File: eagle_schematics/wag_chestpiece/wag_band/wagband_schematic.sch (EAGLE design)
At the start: 8 parts, among them U1 ATMEGA328P_PDIP, U2 TLV1117-33CDCY

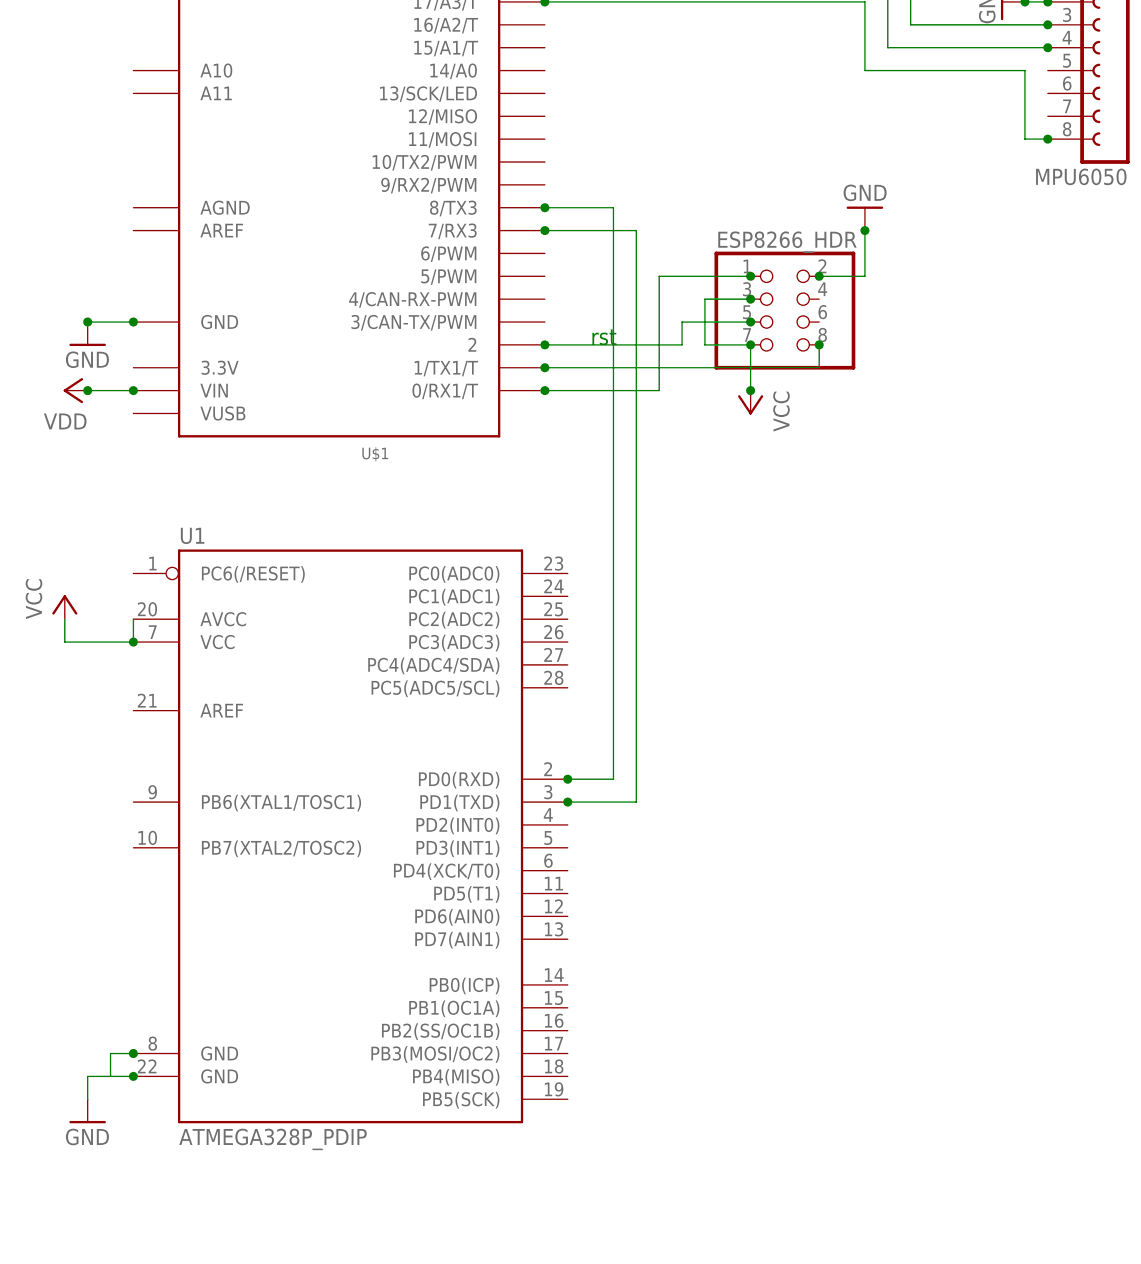
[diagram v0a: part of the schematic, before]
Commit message: Added EasyVR header to chestband
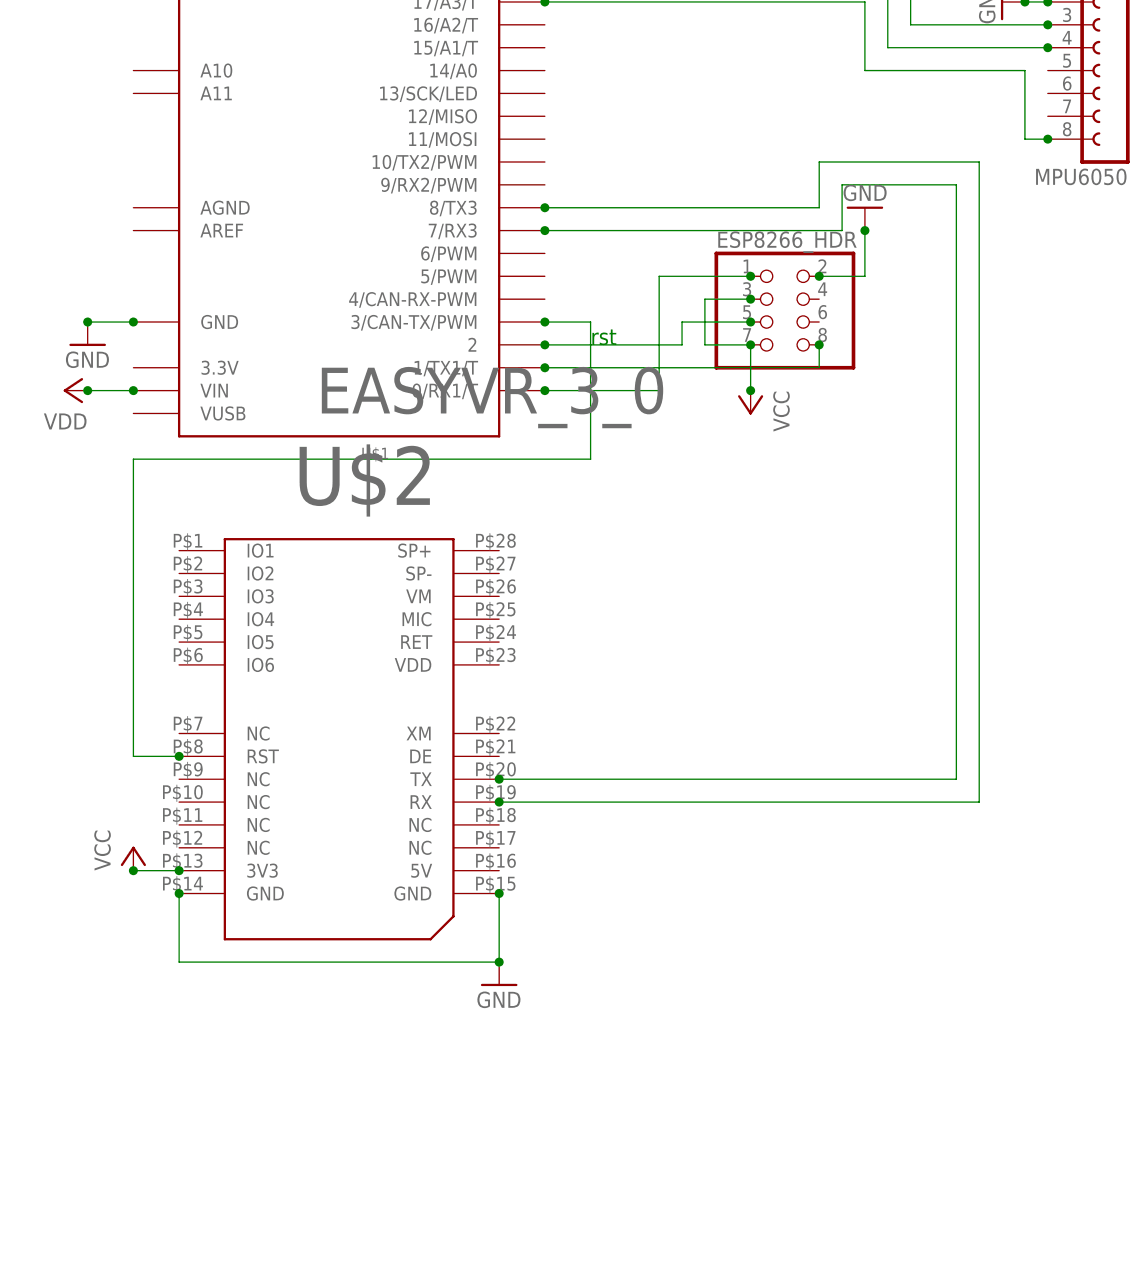
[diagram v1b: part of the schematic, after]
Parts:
- removed U1: ATMEGA328P_PDIP, SparkFun-DigitalIC:ATMEGA328P_PDIP
- added U$2: EASYVR_3_0, mqp_custom_parts:EASYVR_3_0
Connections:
- new net N$5: U$1.3/CAN-TX/PWM, U$2.RST
- net GND: now also U$2.GND@1, U$2.GND@2; no longer U1.GND@1, U1.GND@2
- net N$1: now also U$2.TX; no longer U1.PD1(TXD)
- net N$2: now also U$2.RX; no longer U1.PD0(RXD)
- net VCC: now also U$2.3V3; no longer U1.AVCC, U1.VCC
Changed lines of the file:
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@@
 <part name="GND7" library="supply1" deviceset="GND" device=""/>
 <part name="FRAME1" library="frames" deviceset="A4L-LOC" device="" value="10"/>
-<part name="U1" library="SparkFun-DigitalIC" deviceset="ATMEGA328P_PDIP" device=""/>
-<part name="GND1" library="supply1" deviceset="GND" device=""/>
-<part name="P+5" library="supply1" deviceset="VCC" device=""/>
+<part name="U$2" library="mqp_custom_parts" deviceset="EASYVR_3_0" device=""/>
+<part name="GND8" library="supply1" deviceset="GND" device=""/>
+<part name="P+1" library="supply1" deviceset="VCC" device=""/>
 </parts>
 <sheets>
@@
 <instance part="GND7" gate="1" x="160.02" y="142.24"/>
 <instance part="FRAME1" gate="G$1" x="0" y="0"/>
-<instance part="U1" gate="G$1" x="45.72" y="55.88"/>
-<instance part="GND1" gate="1" x="17.78" y="20.32"/>
-<instance part="P+5" gate="VCC" x="15.24" y="78.74"/>
+<instance part="U$2" gate="G$1" x="45.72" y="66.04"/>
+<instance part="GND8" gate="1" x="63.5" y="35.56"/>
+<instance part="P+1" gate="VCC" x="22.86" y="50.8"/>
 </instances>
 <busses>
@@
 </segment>
 <segment>
-<pinref part="U1" gate="G$1" pin="GND@1"/>
-<junction x="22.86" y="27.94"/>
-<wire x1="22.86" y1="27.94" x2="20.32" y2="27.94" width="0.1524" layer="91"/>
-<wire x1="20.32" y1="27.94" x2="20.32" y2="25.4" width="0.1524" layer="91"/>
-<pinref part="U1" gate="G$1" pin="GND@2"/>
-<junction x="22.86" y="25.4"/>
-<wire x1="20.32" y1="25.4" x2="22.86" y2="25.4" width="0.1524" layer="91"/>
-<wire x1="20.32" y1="25.4" x2="17.78" y2="25.4" width="0.1524" layer="91"/>
-<wire x1="17.78" y1="25.4" x2="17.78" y2="22.86" width="0.1524" layer="91"/>
-<pinref part="GND1" gate="1" pin="GND"/>
+<pinref part="U$2" gate="G$1" pin="GND@2"/>
+<wire x1="63.5" y1="45.72" x2="63.5" y2="38.1" width="0.1524" layer="91"/>
+<wire x1="63.5" y1="38.1" x2="27.94" y2="38.1" width="0.1524" layer="91"/>
+<pinref part="U$2" gate="G$1" pin="GND@1"/>
+<wire x1="27.94" y1="38.1" x2="27.94" y2="45.72" width="0.1524" layer="91"/>
+<junction x="27.94" y="45.72"/>
+<junction x="63.5" y="45.72"/>
+<pinref part="GND8" gate="1" pin="GND"/>
+<junction x="63.5" y="38.1"/>
 </segment>
 </net>
@@
 </segment>
 <segment>
-<pinref part="U1" gate="G$1" pin="VCC"/>
-<junction x="22.86" y="73.66"/>
-<pinref part="U1" gate="G$1" pin="AVCC"/>
-<wire x1="22.86" y1="76.2" x2="22.86" y2="73.66" width="0.1524" layer="91"/>
-<pinref part="P+5" gate="VCC" pin="VCC"/>
-<wire x1="22.86" y1="73.66" x2="15.24" y2="73.66" width="0.1524" layer="91"/>
-<wire x1="15.24" y1="73.66" x2="15.24" y2="76.2" width="0.1524" layer="91"/>
+<pinref part="P+1" gate="VCC" pin="VCC"/>
+<pinref part="U$2" gate="G$1" pin="3V3"/>
+<wire x1="22.86" y1="48.26" x2="27.94" y2="48.26" width="0.1524" layer="91"/>
+<junction x="22.86" y="48.26"/>
+<junction x="27.94" y="48.26"/>
 </segment>
 </net>
@@
 <segment>
 <pinref part="U$1" gate="G$1" pin="7/RX3"/>
-<wire x1="68.58" y1="119.38" x2="78.74" y2="119.38" width="0.1524" layer="91"/>
-<wire x1="78.74" y1="119.38" x2="78.74" y2="55.88" width="0.1524" layer="91"/>
-<pinref part="U1" gate="G$1" pin="PD1(TXD)"/>
-<wire x1="78.74" y1="55.88" x2="71.12" y2="55.88" width="0.1524" layer="91"/>
 <junction x="68.58" y="119.38"/>
-<junction x="71.12" y="55.88"/>
+<wire x1="68.58" y1="119.38" x2="101.6" y2="119.38" width="0.1524" layer="91"/>
+<wire x1="101.6" y1="119.38" x2="101.6" y2="124.46" width="0.1524" layer="91"/>
+<wire x1="101.6" y1="124.46" x2="114.3" y2="124.46" width="0.1524" layer="91"/>
+<wire x1="114.3" y1="124.46" x2="114.3" y2="58.42" width="0.1524" layer="91"/>
+<wire x1="114.3" y1="58.42" x2="63.5" y2="58.42" width="0.1524" layer="91"/>
+<pinref part="U$2" gate="G$1" pin="TX"/>
+<junction x="63.5" y="58.42"/>
 </segment>
 </net>
@@
 <segment>
 <pinref part="U$1" gate="G$1" pin="8/TX3"/>
-<wire x1="68.58" y1="121.92" x2="76.2" y2="121.92" width="0.1524" layer="91"/>
-<wire x1="76.2" y1="121.92" x2="76.2" y2="58.42" width="0.1524" layer="91"/>
-<pinref part="U1" gate="G$1" pin="PD0(RXD)"/>
-<wire x1="76.2" y1="58.42" x2="71.12" y2="58.42" width="0.1524" layer="91"/>
 <junction x="68.58" y="121.92"/>
-<junction x="71.12" y="58.42"/>
-</segment>
-</net>
+<wire x1="68.58" y1="121.92" x2="99.06" y2="121.92" width="0.1524" layer="91"/>
+<wire x1="99.06" y1="121.92" x2="99.06" y2="127" width="0.1524" layer="91"/>
+<wire x1="99.06" y1="127" x2="116.84" y2="127" width="0.1524" layer="91"/>
+<wire x1="116.84" y1="127" x2="116.84" y2="55.88" width="0.1524" layer="91"/>
+<pinref part="U$2" gate="G$1" pin="RX"/>
+<wire x1="116.84" y1="55.88" x2="63.5" y2="55.88" width="0.1524" layer="91"/>
+<junction x="63.5" y="55.88"/>
+</segment>
+</net>
+<net name="N$5" class="0">
+<segment>
+<pinref part="U$1" gate="G$1" pin="3/CAN-TX/PWM"/>
+<junction x="68.58" y="109.22"/>
+<wire x1="68.58" y1="109.22" x2="73.66" y2="109.22" width="0.1524" layer="91"/>
+<wire x1="73.66" y1="109.22" x2="73.66" y2="93.98" width="0.1524" layer="91"/>
+<wire x1="73.66" y1="93.98" x2="22.86" y2="93.98" width="0.1524" layer="91"/>
+<wire x1="22.86" y1="93.98" x2="22.86" y2="60.96" width="0.1524" layer="91"/>
+<pinref part="U$2" gate="G$1" pin="RST"/>
+<junction x="27.94" y="60.96"/>
+<wire x1="22.86" y1="60.96" x2="27.94" y2="60.96" width="0.1524" layer="91"/>
+</segment>
+</net>

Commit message: Added more parts for eagle
Finished PCBs
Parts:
- removed BATTERY: (no value), adafruit:JST_2PIN-THM-RA
- removed ESP8266_HDR: (no value), pinhead:PINHD-2X4
- removed MPU6050: (no value), con-lsta:FE08-1
- added BAT, CHGR: (no value), adafruit:JST_2PIN-THM-RA
- added C3, C4: 22pF, rcl:C-USC1206K
- added LED1, PWR: (no value), led:LED5MM
- added MPU6050_BREAKOUT: (no value), mqp_custom_parts:MPU6050_BREAKOUT
- added Q1, Q2: (no value), mqp_custom_parts:TRANSISTOR_NPNMMBT3904
- added R1, R4: 1k, resistor:R-US_R1206
- added R2, R3: 30k, resistor:R-US_R1206
- added R5: 10k, resistor:R-US_R1206
- added U$3: CB10LV103M, mqp_custom_parts:CB10LV103M
- added U$4: ESP01, esp8266modules:ESP01
- added U$5: MS12ASW13, mqp_custom_parts:MS12ASW13
- added U1: ATMEGA328P_PDIP, SparkFun-DigitalIC:ATMEGA328P_PDIP
- added U3: LM358DR, Texas Instruments_By_element14_Batch_1:LM358DR
- added Y1: 16MHz, SparkFun-FreqCtrl:CRYSTALSMD
- C1, C2: device rcl:C-EU025-024X044 -> resistor:C-USC0805K
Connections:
- new net !RST: R5.1, U$1.2, U$2.RST, U$4.CH_PD, U1.PC6(/RESET)
- new net N$10: Q2.C, R1.1, U3.1IN+
- new net N$11: R3.1, U$3.B
- new net N$12: LED1.C, R1.2
- new net N$13: U$1.1/TX1/T, U1.PD0(RXD)
- new net N$14: U$1.16/A2/T, U3.1OUT
- new net N$15: PWR.C, R4.2
- new net N$16: U$1.3/CAN-TX/PWM, U1.PD7(AIN1)
- new net N$18: U$1.6/PWM, U$4.GPIO2
- new net N$20: C3.1, U1.PB6(XTAL1/TOSC1), Y1.2
- new net N$22: U$1.0/RX1/T, U1.PD1(TXD)
- new net N$23: BAT.2, U$5.P$2
- new net N$25: CHGR.2, U$5.P$3
- new net N$3: MPU6050_BREAKOUT.SDA, U$1.18/A4/T/SDA0
- new net N$6: U$2.TX, U1.PD4(XCK/T0)
- new net N$9: Q1.C, Q2.B, R2.1
- net GND: now also BAT.1, C3.2, C4.2, CHGR.1, MPU6050_BREAKOUT.GND, Q1.E, Q2.E, R4.1, U$3.A, U$4.GND, U1.GND@1, U1.GND@2, U3.GND; no longer BATTERY.2, ESP8266_HDR.2, MPU6050.2
- net N$1: now also U$1.4/CAN-RX-PWM, U1.PD2(INT0); no longer U$1.7/RX3, U$2.TX
- net N$17: now also MPU6050_BREAKOUT.SCL; no longer MPU6050.3
- net N$19: now also U$1.9/RX2/PWM, U$4.TXD; no longer ESP8266_HDR.8, U$1.1/TX1/T
- net N$2: now also U$1.10/TX2/PWM, U$4.RXD; no longer U$1.8/TX3, U$2.RX
- net N$21: now also C4.1, U1.PB7(XTAL2/TOSC2), Y1.1; no longer ESP8266_HDR.5, U$1.2
- net N$4: now also Q1.B, U$3.C, U3.1IN-; no longer MPU6050.4, U$1.18/A4/T/SDA0
- net N$5: now also U$2.RX, U1.PD5(T1); no longer U$1.3/CAN-TX/PWM, U$2.RST
- net N$7: now also U$1.5/PWM, U$4.GPIO0; no longer ESP8266_HDR.1, U$1.0/RX1/T
- net N$8: now also MPU6050_BREAKOUT.INT; no longer MPU6050.8
- net VCC: now also LED1.A, MPU6050_BREAKOUT.VCC, PWR.A, R2.2, R3.2, R5.2, U$4.RST, U$4.VCC, U$5.P$1, U1.VCC, U3.VCC; no longer BATTERY.1, ESP8266_HDR.3, ESP8266_HDR.7, MPU6050.1
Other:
- note added: "!rst"
- note removed: "rst"
- moved on the sheet: C1, C2, U$2, U2

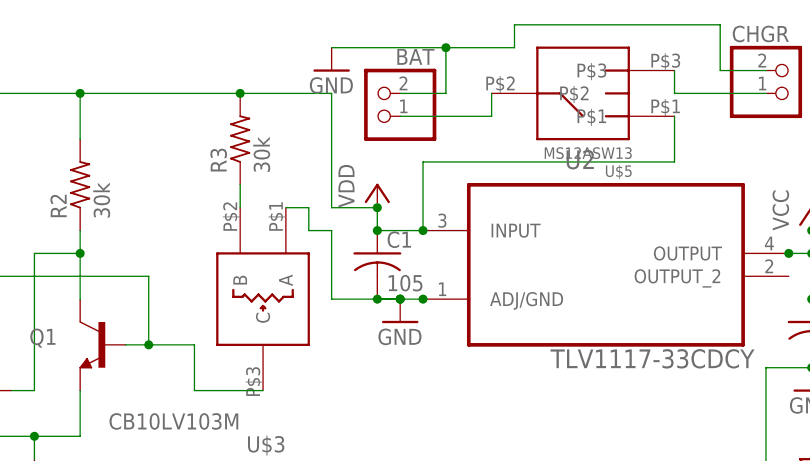
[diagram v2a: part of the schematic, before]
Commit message: Eagle schematic for chestpiece
Added new chestpiece with larger traces and everything good
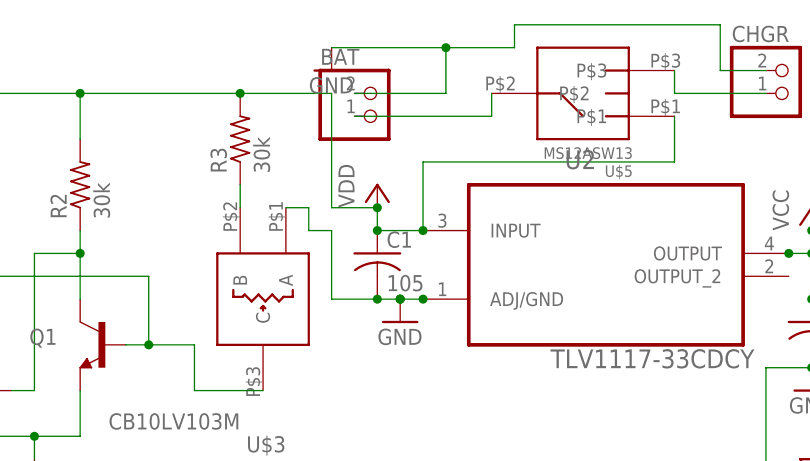
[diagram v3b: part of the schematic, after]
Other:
- moved on the sheet: BAT
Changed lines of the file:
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@@
 <part name="Q1" library="mqp_custom_parts" deviceset="TRANSISTOR_NPN" device="MMBT3904"/>
 <part name="Q2" library="mqp_custom_parts" deviceset="TRANSISTOR_NPN" device="MMBT3904"/>
-<part name="U$3" library="mqp_custom_parts" deviceset="CB10LV103M" device=""/>
 <part name="U3" library="Texas Instruments_By_element14_Batch_1" deviceset="LM358DR" device=""/>
 <part name="GND9" library="supply1" deviceset="GND" device=""/>
@@
 <part name="U$5" library="mqp_custom_parts" deviceset="MS12ASW13" device=""/>
 <part name="CHGR" library="adafruit" deviceset="JST_2PIN" device="-THM-RA"/>
+<part name="U$3" library="mqp_custom_parts" deviceset="CB10LV103M" device=""/>
 </parts>
 <sheets>
@@
 <instance part="P+4" gate="VCC" x="111.76" y="134.62"/>
 <instance part="GND6" gate="1" x="76.2" y="114.3"/>
-<instance part="BAT" gate="G$1" x="200.66" y="165.1" rot="MR0"/>
+<instance part="BAT" gate="G$1" x="200.66" y="165.1"/>
 <instance part="GND7" gate="1" x="195.58" y="170.18"/>
 <instance part="FRAME1" gate="G$1" x="0" y="0"/>
@@
 <instance part="Q1" gate="G$1" x="170.18" y="139.7" rot="MR0"/>
 <instance part="Q2" gate="G$1" x="157.48" y="134.62" rot="MR0"/>
-<instance part="U$3" gate="G$1" x="187.96" y="144.78" rot="R180"/>
 <instance part="U3" gate="A" x="127" y="147.32" rot="MR0"/>
 <instance part="GND9" gate="1" x="162.56" y="124.46"/>
@@
 <instance part="U$5" gate="G$1" x="226.06" y="167.64" rot="R180"/>
 <instance part="CHGR" gate="G$1" x="246.38" y="167.64"/>
+<instance part="U$3" gate="G$1" x="187.96" y="144.78" rot="R180"/>
 </instances>
 <busses>
@@
 <pinref part="C1" gate="G$1" pin="2"/>
 <junction x="203.2" y="144.78"/>
-<wire x1="200.66" y1="144.78" x2="203.2" y2="144.78" width="0.1524" layer="91"/>
-<pinref part="U$3" gate="G$1" pin="A"/>
 <wire x1="190.5" y1="154.94" x2="193.04" y2="154.94" width="0.1524" layer="91"/>
 <wire x1="193.04" y1="154.94" x2="193.04" y2="152.4" width="0.1524" layer="91"/>
@@
 <junction x="200.66" y="144.78"/>
 <wire x1="200.66" y1="144.78" x2="203.2" y2="144.78" width="0.1524" layer="91"/>
+<pinref part="U$3" gate="G$1" pin="A"/>
 </segment>
 <segment>
@@
 <wire x1="208.28" y1="172.72" x2="208.28" y2="167.64" width="0.1524" layer="91"/>
 <pinref part="BAT" gate="G$1" pin="1"/>
-<wire x1="208.28" y1="167.64" x2="203.2" y2="167.64" width="0.1524" layer="91"/>
+<wire x1="208.28" y1="167.64" x2="198.12" y2="167.64" width="0.1524" layer="91"/>
 <wire x1="208.28" y1="172.72" x2="215.9" y2="172.72" width="0.1524" layer="91"/>
 <wire x1="215.9" y1="172.72" x2="215.9" y2="175.26" width="0.1524" layer="91"/>
@@
 <wire x1="175.26" y1="139.7" x2="180.34" y2="139.7" width="0.1524" layer="91"/>
 <wire x1="180.34" y1="139.7" x2="180.34" y2="134.62" width="0.1524" layer="91"/>
-<pinref part="U$3" gate="G$1" pin="C"/>
 <wire x1="180.34" y1="134.62" x2="187.96" y2="134.62" width="0.1524" layer="91"/>
 <pinref part="U3" gate="A" pin="1IN-"/>
@@
 <junction x="144.78" y="147.32"/>
 <junction x="175.26" y="139.7"/>
+<pinref part="U$3" gate="G$1" pin="C"/>
 </segment>
 </net>
 <net name="N$11" class="0">
 <segment>
-<pinref part="U$3" gate="G$1" pin="B"/>
 <pinref part="R3" gate="G$1" pin="1"/>
 <wire x1="185.42" y1="154.94" x2="185.42" y2="157.48" width="0.1524" layer="91"/>
+<pinref part="U$3" gate="G$1" pin="B"/>
 </segment>
 </net>
@@
 <pinref part="BAT" gate="G$1" pin="2"/>
 <pinref part="U$5" gate="G$1" pin="P$2"/>
-<wire x1="203.2" y1="165.1" x2="213.36" y2="165.1" width="0.1524" layer="91"/>
+<wire x1="198.12" y1="165.1" x2="213.36" y2="165.1" width="0.1524" layer="91"/>
 <wire x1="213.36" y1="165.1" x2="213.36" y2="167.64" width="0.1524" layer="91"/>
 </segment>
